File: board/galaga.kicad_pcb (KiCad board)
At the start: 2 copper layers, 119.4 x 48.3 mm, 20 parts, among them J1 led_a, J2 speaker_out, J3 led_b, J4 led_c, J5 pwr_in, U1 LD1117S33TR_SOT223, U2 ATmega328P-PU, U3 LM386, U4 BOB-00544

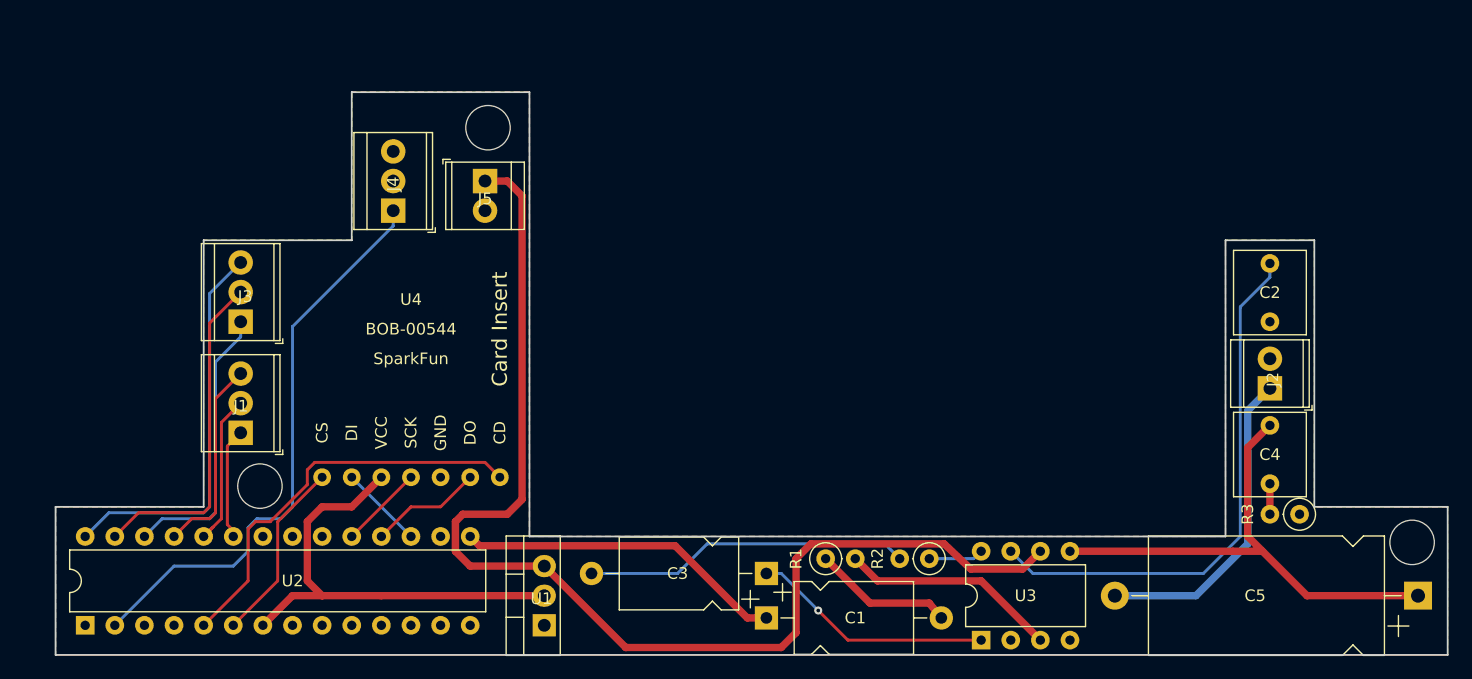
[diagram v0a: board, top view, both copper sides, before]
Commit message: changed SD CS pin to PORTB7 for better board layout
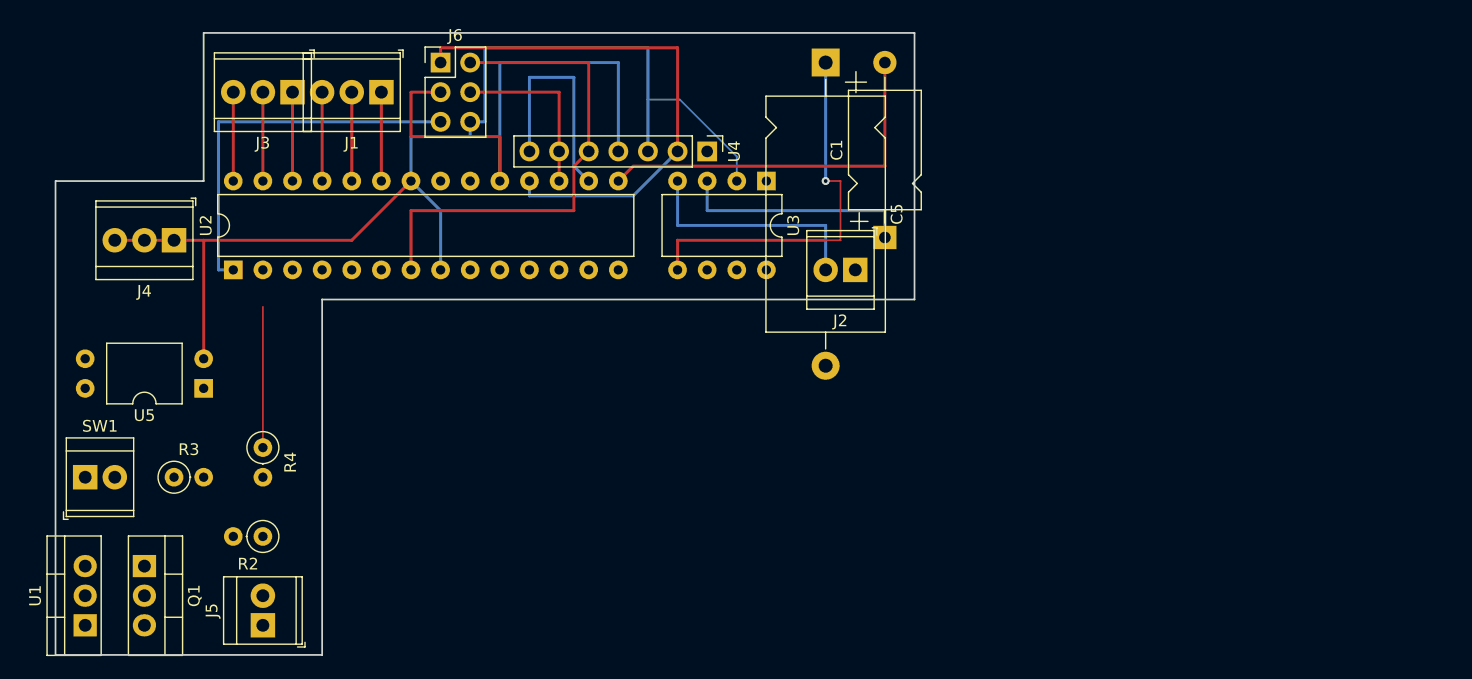
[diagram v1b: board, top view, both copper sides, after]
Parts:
- removed C2: 0.5uF, Capacitor_THT:C_Rect_L7.0mm_W6.0mm_P5.00mm
- removed C3: 10uF, Capacitor_THT:CP_Axial_L10.0mm_D6.0mm_P15.00mm_Horizontal
- removed C4: 0.05uF, Capacitor_THT:C_Rect_L7.0mm_W6.0mm_P5.00mm
- removed R1: 10k (max), Resistor_THT:R_Axial_DIN0207_L6.3mm_D2.5mm_P2.54mm_Vertical
- removed REF** (x3): mount_hole, custom:mount_hole
- added J6: Conn_02x03_Odd_Even, Connector_PinHeader_2.54mm:PinHeader_2x03_P2.54mm_Vertical, F.Cu at (58.4, 127.0)
- added Q1: 2N7000, Package_TO_SOT_THT:TO-220-3_Vertical, F.Cu at (33.0, 170.2)
- added R4: 180R, Resistor_THT:R_Axial_DIN0207_L6.3mm_D2.5mm_P2.54mm_Vertical, F.Cu at (43.2, 160.0)
- added SW1: SW_Push, TerminalBlock_TE-Connectivity:TerminalBlock_TE_282834-2_1x02_P2.54mm_Horizontal, F.Cu at (27.9, 162.6)
- added U5: LTV-817M, Package_DIP:DIP-4_W10.16mm, F.Cu at (38.1, 154.9)
- R2: value 10k (max) -> 10M
- R3: value 10 -> 20K
- U4: footprint custom:bob-00544 -> Connector_PinHeader_2.54mm:PinHeader_1x07_P2.54mm_Vertical
- moved R3 96.6 mm to (35.6, 162.6), turned to 0 degrees
- moved C5 68.3 mm to (91.4, 127.0), turned to 270 degrees
- moved R2 57.2 mm to (43.2, 167.6)
- moved U3 43.5 mm to (86.4, 137.2), turned to 270 degrees
- moved J5 42.6 mm to (43.2, 175.3), turned to 90 degrees
- moved U1 39.4 mm to (27.9, 175.3)
- moved J2 37.0 mm to (94.0, 144.8), turned to 180 degrees
- moved C1 34.2 mm to (96.5, 142.0), turned to 90 degrees
- moved U2 33.0 mm to (40.6, 144.8)
- moved J1 31.6 mm to (53.3, 129.5), turned to 180 degrees
- moved U4 31.0 mm to (81.3, 134.6), turned to 270 degrees
- moved J3 20.2 mm to (45.7, 129.5), turned to 180 degrees
- moved J4 19.0 mm to (35.6, 142.2), turned to 180 degrees
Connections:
- J2 pad 2: GND -> BGND
- J4 pad 1: Net-(J4-Pad1) -> DGND
- J4 pad 2: GND -> DGND
- J4 pad 3: GND -> DGND
- J5 pad 2: GND -> BGND
- R2 pad 1: Net-(R2-Pad1) -> +9V
- R2 pad 2: Net-(C3-Pad2) -> DGND
- R3 pad 1: GND -> Net-(R3-Pad1)
- U1 pad 1: GND -> DGND
- U2 pad 15: Net-(C1-Pad1) -> Net-(C1-Pad2)
- U2 pad 16: Net-(U2-Pad16) -> /sd_cs
- U2 pad 2: Net-(J4-Pad1) -> Net-(U2-Pad2)
- U2 pad 22: GND -> DGND
- U2 pad 5: /sd_cd -> Net-(U2-Pad5)
- U2 pad 6: /sd_cs -> Net-(U2-Pad6)
- U2 pad 8: GND -> DGND
- U2 pad 9: Net-(U2-Pad9) -> PWR_OFF
- U3 pad 2: GND -> DGND
- U3 pad 3: Net-(R1-Pad2) -> Net-(C1-Pad1)
- U3 pad 4: GND -> BGND
- U3 pad 8: Net-(R2-Pad1) -> Net-(U3-Pad8)
- U4 pad 1: /sd_cd -> Net-(U4-Pad1)
- U4 pad 3: GND -> DGND
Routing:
- net +9V: track 101.3 -> 0.00 mm
- net DGND: track 0.00 -> 98.7 mm
- net Net-(J4-Pad1): track 50.8 -> 0.00 mm
- net Net-(U3-Pad7): track 46.3 -> 0.00 mm
- net /sd_sck: track 7.18 -> 45.7 mm
- net /sd_do: track 9.72 -> 46.0 mm
- net /sd_cd: track 35.1 -> 0.00 mm
- net Net-(J6-Pad5): track 0.00 -> 33.0 mm
- net Net-(C3-Pad2): track 28.0 -> 0.00 mm
- net Net-(C5-Pad2): track 28.0 -> 0.00 mm
- net /led_bs1: track 33.8 -> 7.62 mm
- net /led_bl2: track 32.2 -> 7.62 mm
- net /led_bl3: track 28.7 -> 7.62 mm
- net Net-(U3-Pad1): track 20.8 -> 0.00 mm, vias 1 -> 0
- net BGND: track 0.00 -> 20.3 mm
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- removed copper zone on F.Cu, net (none)
- removed copper zone on B.Cu, net GND
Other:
- board size 119.4 x 48.3 mm -> 73.7 x 53.3 mm
- board text removed: "Galaga V1.0 N Piscitello 2018-10"
- board text removed: "keep 3v3 away from sck di will have very little (if any) traffic"
